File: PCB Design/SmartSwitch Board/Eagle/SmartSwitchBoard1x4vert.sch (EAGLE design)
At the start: 40 parts, among them IC1 MCP23017SS, IC2 PCA9685

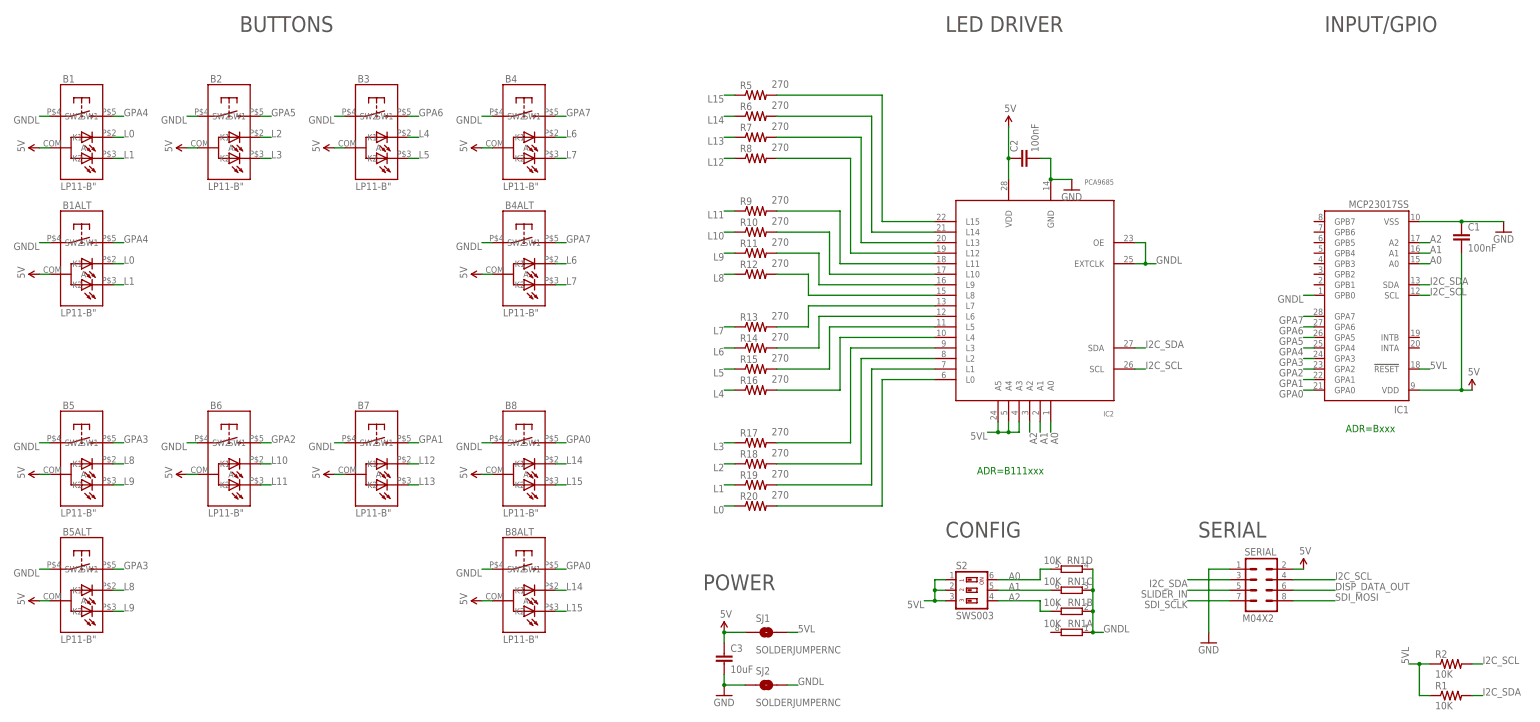
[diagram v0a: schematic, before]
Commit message: Lots of updates to PCBs, adding new headers, updated schematics, switches shorting to GND
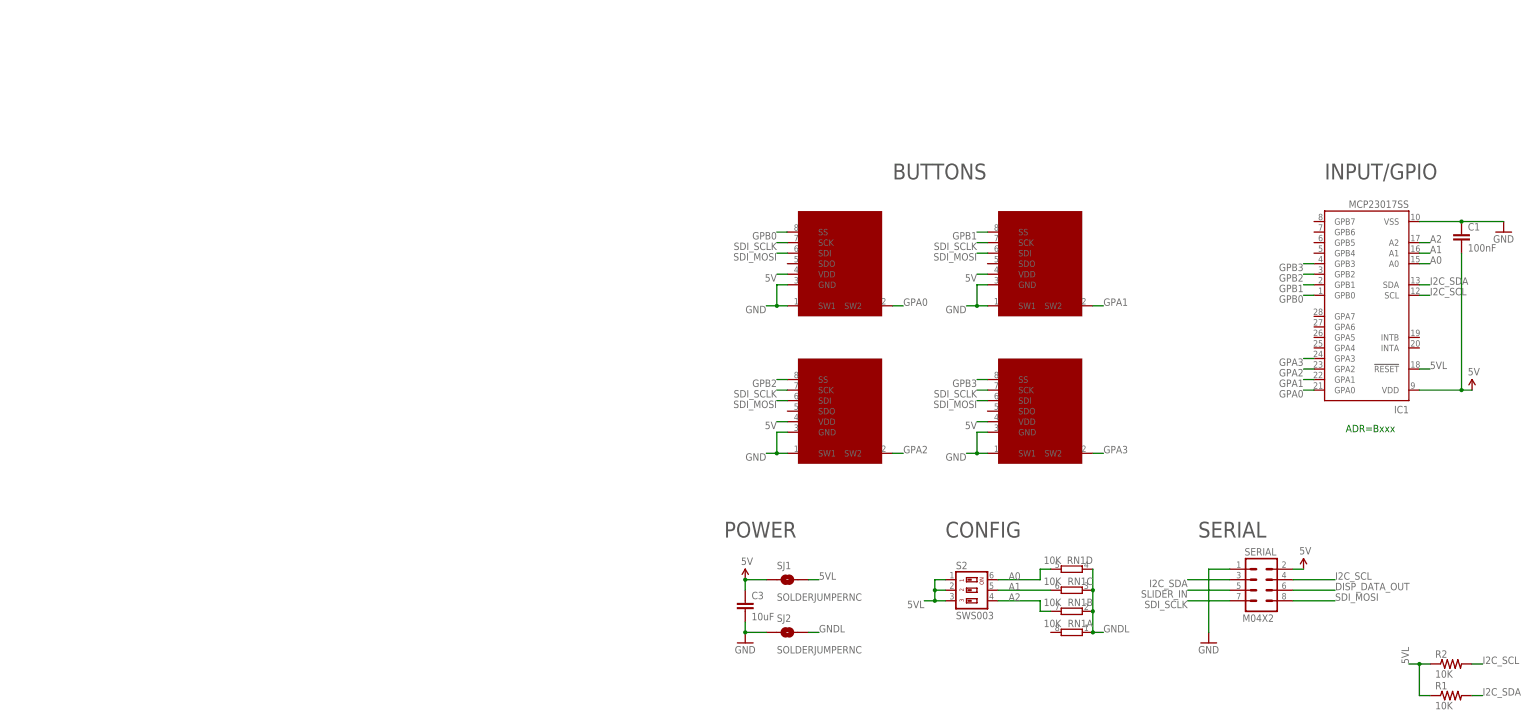
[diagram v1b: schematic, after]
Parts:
- removed B1, B1ALT, B2, B3, B4, B4ALT, B5, B5ALT, B6, B7, B8, B8ALT: LP11-B", SKAARHOJ:LP11-B"
- removed C2: 100nF, SparkFun:CAP0603-CAP
- removed IC2: PCA9685, wsmith:PCA9685
- removed R10, R11, R12, R13, R14, R15, R16, R17, R18, R19, R20, R5, R6, R7, R8, R9: 270, SparkFun:RESISTOR0603-RES
- added U$2, U$3, U$4, U$5: SMART_SWITCHSMART_SWITCH_8PIN, SKAARHOJ:SMART_SWITCHSMART_SWITCH_8PIN
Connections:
- removed net GPA4: B1.SW2, B1ALT.SW2, IC1.GPA4
- removed net GPA5: B2.SW2, IC1.GPA5
- removed net GPA6: B3.SW2, IC1.GPA6
- removed net GPA7: B4.SW2, B4ALT.SW2, IC1.GPA7
- removed net L0: B1.K1, B1ALT.K1, R20.1
- removed net L1: B1.K2, B1ALT.K2, R19.1
- removed net L10: B6.K1, R10.1
- removed net L11: B6.K2, R9.1
- removed net L12: B7.K1, R8.1
- removed net L13: B7.K2, R7.1
- removed net L14: B8.K1, B8ALT.K1, R6.1
- removed net L15: B8.K2, B8ALT.K2, R5.1
- removed net L2: B2.K1, R18.1
- removed net L3: B2.K2, R17.1
- removed net L4: B3.K1, R16.1
- removed net L5: B3.K2, R15.1
- removed net L6: B4.K1, B4ALT.K1, R14.1
- removed net L7: B4.K2, B4ALT.K2, R13.1
- removed net L8: B5.K1, B5ALT.K1, R12.1
- removed net L9: B5.K2, B5ALT.K2, R11.1
- removed net N$10: IC2.L3, R17.2
- removed net N$11: IC2.L2, R18.2
- removed net N$12: IC2.L1, R19.2
- removed net N$19: IC2.L0, R20.2
- removed net N$20: IC2.L8, R12.2
- removed net N$21: IC2.L9, R11.2
- removed net N$22: IC2.L10, R10.2
- removed net N$23: IC2.L11, R9.2
- removed net N$24: IC2.L12, R8.2
- removed net N$25: IC2.L13, R7.2
- removed net N$26: IC2.L14, R6.2
- removed net N$27: IC2.L15, R5.2
- removed net N$4: IC2.L7, R13.2
- removed net N$5: IC2.L6, R14.2
- removed net N$7: IC2.L5, R15.2
- removed net N$9: IC2.L4, R16.2
- new net GPB0: IC1.GPB0, U$2.SS
- new net GPB1: IC1.GPB1, U$3.SS
- new net GPB2: IC1.GPB2, U$4.SS
- new net GPB3: IC1.GPB3, U$5.SS
- net 5V: now also U$2.VDD, U$3.VDD, U$4.VDD, U$5.VDD; no longer B1.A, B1ALT.A, B2.A, B3.A, B4.A, B4ALT.A, B5.A, B5ALT.A, B6.A, B7.A, B8.A, B8ALT.A, C2.1, IC2.VDD
- net 5VL: no longer IC2.A3, IC2.A4, IC2.A5
- net A0: no longer IC2.A0
- net A1: no longer IC2.A1
- net A2: no longer IC2.A2
- net GND: now also U$2.GND, U$2.SW1, U$3.GND, U$3.SW1, U$4.GND, U$4.SW1, U$5.GND, U$5.SW1; no longer C2.2, IC2.GND
- net GNDL: no longer B1.SW1, B1ALT.SW1, B2.SW1, B3.SW1, B4.SW1, B4ALT.SW1, B5.SW1, B5ALT.SW1, B6.SW1, B7.SW1, B8.SW1, B8ALT.SW1, IC1.GPB0, IC2.EXTCLK, IC2.OE
- net GPA0: now also U$2.SW2; no longer B8.SW2, B8ALT.SW2
- net GPA1: now also U$3.SW2; no longer B7.SW2
- net GPA2: now also U$4.SW2; no longer B6.SW2
- net GPA3: now also U$5.SW2; no longer B5.SW2, B5ALT.SW2
- net I2C_SCL: no longer IC2.SCL
- net I2C_SDA: no longer IC2.SDA
- net SDI_MOSI: now also U$2.SDI, U$3.SDI, U$4.SDI, U$5.SDI
- net SDI_SCLK: now also U$2.SCK, U$3.SCK, U$4.SCK, U$5.SCK
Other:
- note removed: "ADR=B111xxx"
- note removed: "LED DRIVER"
- moved on the sheet: C3, SJ1, SJ2
